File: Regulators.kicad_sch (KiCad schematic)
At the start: 22 parts, among them J5 24V Logic, J6 24V Isolated, U2 XL1509-12, U3 XL1509-5.0

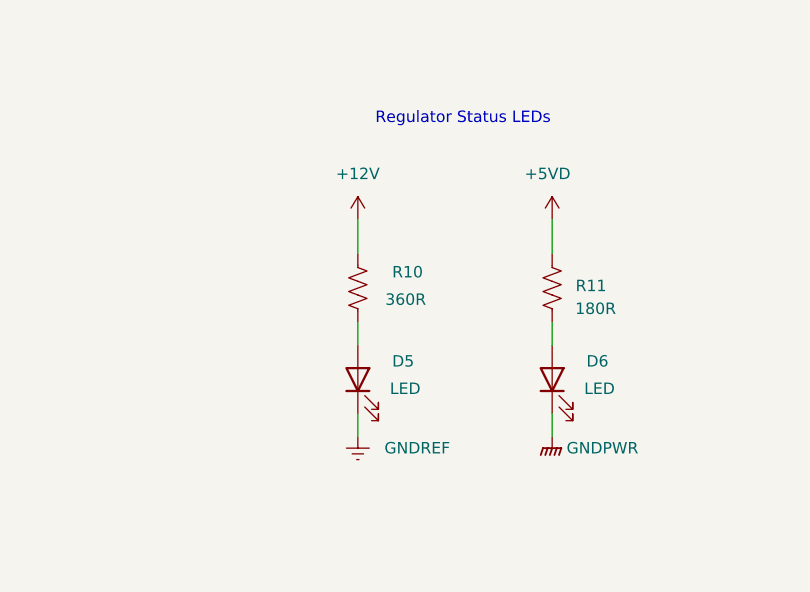
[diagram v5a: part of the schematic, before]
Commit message: Caught some errors with spacing of jumpers, did some BOM consolidation and included BOM. Updates to Gerbers to reflect new changes.
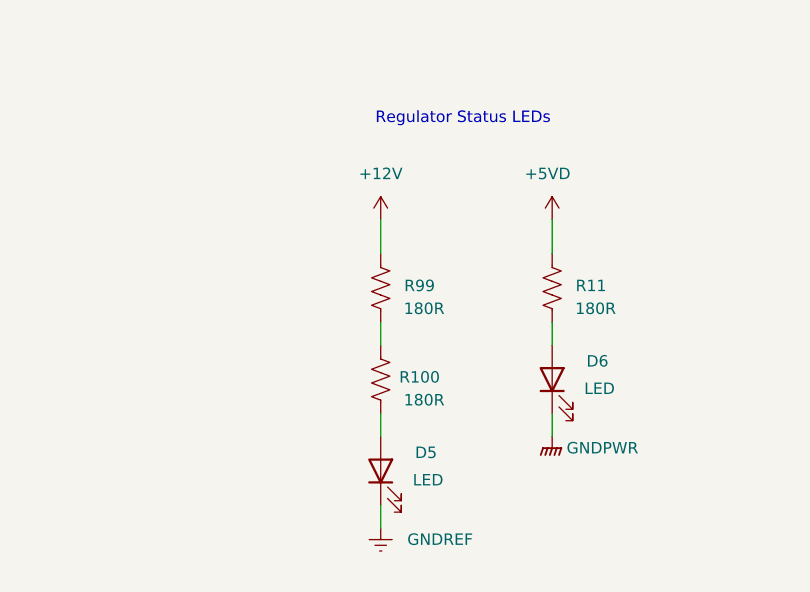
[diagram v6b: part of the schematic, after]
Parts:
- removed R10: 360R, Resistor_SMD:R_1206_3216Metric_Pad1.30x1.75mm_HandSolder, symbol Device:R_US
- added R100, R99: 180R, Resistor_SMD:R_1206_3216Metric_Pad1.30x1.75mm_HandSolder, symbol Device:R_US
- C3, C4: Digikey Part Number 493-12789-1-ND -> 493-1110-ND; Digikey URL https://www.digikey.com.au/en/products/detail/nichicon/UVR1H471MHD1TO/1978711 -> https://www.digikey.com.au/en/products/detail/nichicon/UVR1H471MHD/588851
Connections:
- net +12V: now also R99.1
- net at D5.2 (A): now also R100.2
- new net: R100.1, R99.2
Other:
- moved on the sheet: D5
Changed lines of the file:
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@@
 	(wire
 		(pts
+			(xy 217.17 120.65) (xy 217.17 123.19)
+		)
+		(stroke
+			(width 0)
+			(type default)
+		)
+	)
+	(wire
+		(pts
 			(xy 153.67 107.95) (xy 153.67 109.22)
 		)
@@
 	(wire
 		(pts
-			(xy 214.63 109.22) (xy 214.63 113.03)
+			(xy 217.17 109.22) (xy 217.17 113.03)
 		)
 		(stroke
@@
 	(wire
 		(pts
-			(xy 214.63 130.81) (xy 214.63 133.35)
+			(xy 217.17 140.97) (xy 217.17 143.51)
 		)
 		(stroke
@@
 	(wire
 		(pts
-			(xy 214.63 120.65) (xy 214.63 123.19)
+			(xy 217.17 130.81) (xy 217.17 133.35)
 		)
 		(stroke
@@
 	(symbol
 		(lib_id "power:+12V")
-		(at 214.63 109.22 0)
+		(at 217.17 109.22 0)
 		(unit 1)
 		(exclude_from_sim no)
@@
 		(fields_autoplaced yes)
 		(property "Reference" "#PWR054"
-			(at 214.63 113.03 0)
+			(at 217.17 113.03 0)
 			(effects
 				(font
@@
 		)
 		(property "Value" "+12V"
-			(at 214.63 104.14 0)
+			(at 217.17 104.14 0)
 			(effects
 				(font
@@
 		)
 		(property "Footprint" ""
-			(at 214.63 109.22 0)
+			(at 217.17 109.22 0)
 			(effects
 				(font
@@
 		)
 		(property "Datasheet" ""
-			(at 214.63 109.22 0)
+			(at 217.17 109.22 0)
 			(effects
 				(font
@@
 		)
 		(property "Description" "Power symbol creates a global label with name \"+12V\""
-			(at 214.63 109.22 0)
+			(at 217.17 109.22 0)
 			(effects
 				(font
@@
 	)
 	(symbol
+		(lib_id "Device:R_US")
+		(at 217.17 116.84 0)
+		(unit 1)
+		(exclude_from_sim no)
+		(in_bom yes)
+		(on_board yes)
+		(dnp no)
+		(property "Reference" "R99"
+			(at 221.488 116.586 0)
+			(effects
+				(font
+					(size 1.27 1.27)
+				)
+			)
+		)
+		(property "Value" "180R"
+			(at 221.996 119.126 0)
+			(effects
+				(font
+					(size 1.27 1.27)
+				)
+			)
+		)
+		(property "Footprint" "Resistor_SMD:R_1206_3216Metric_Pad1.30x1.75mm_HandSolder"
+			(at 218.186 117.094 90)
+			(effects
+				(font
+					(size 1.27 1.27)
+				)
+				(hide yes)
+			)
+		)
+		(property "Datasheet" "~"
+			(at 217.17 116.84 0)
+			(effects
+				(font
+					(size 1.27 1.27)
+				)
+				(hide yes)
+			)
+		)
+		(property "Description" "Resistor, US symbol"
+			(at 217.17 116.84 0)
+			(effects
+				(font
+					(size 1.27 1.27)
+				)
+				(hide yes)
+			)
+		)
+		(property "Digikey Part Number" "311-180FRCT-ND"
+			(at 217.17 116.84 0)
+			(effects
+				(font
+					(size 1.27 1.27)
+				)
+				(hide yes)
+			)
+		)
+		(property "Digikey URL" "https://www.digikey.com.au/en/products/detail/yageo/RC1206FR-07180RL/728597"
+			(at 217.17 116.84 0)
+			(effects
+				(font
+					(size 1.27 1.27)
+				)
+				(hide yes)
+			)
+		)
+		(pin "2"
+		)
+		(pin "1"
+		)
+		(instances
+			(project "Remora Nucleo F446ZE Hat"
+				(path "/5473abc6-7b93-43cc-a401-f691c4d7d7cf/e0dc83df-f7d9-4488-bd0b-6c0af36f8703"
+					(reference "R99")
+					(unit 1)
+				)
+			)
+		)
+	)
+	(symbol
 		(lib_id "power:+5VD")
 		(at 153.67 107.95 0)
@@
 	)
 	(symbol
+		(lib_id "Device:R_US")
+		(at 217.17 127 0)
+		(unit 1)
+		(exclude_from_sim no)
+		(in_bom yes)
+		(on_board yes)
+		(dnp no)
+		(property "Reference" "R100"
+			(at 221.488 126.746 0)
+			(effects
+				(font
+					(size 1.27 1.27)
+				)
+			)
+		)
+		(property "Value" "180R"
+			(at 221.996 129.286 0)
+			(effects
+				(font
+					(size 1.27 1.27)
+				)
+			)
+		)
+		(property "Footprint" "Resistor_SMD:R_1206_3216Metric_Pad1.30x1.75mm_HandSolder"
+			(at 218.186 127.254 90)
+			(effects
+				(font
+					(size 1.27 1.27)
+				)
+				(hide yes)
+			)
+		)
+		(property "Datasheet" "~"
+			(at 217.17 127 0)
+			(effects
+				(font
+					(size 1.27 1.27)
+				)
+				(hide yes)
+			)
+		)
+		(property "Description" "Resistor, US symbol"
+			(at 217.17 127 0)
+			(effects
+				(font
+					(size 1.27 1.27)
+				)
+				(hide yes)
+			)
+		)
+		(property "Digikey Part Number" "311-180FRCT-ND"
+			(at 217.17 127 0)
+			(effects
+				(font
+					(size 1.27 1.27)
+				)
+				(hide yes)
+			)
+		)
+		(property "Digikey URL" "https://www.digikey.com.au/en/products/detail/yageo/RC1206FR-07180RL/728597"
+			(at 217.17 127 0)
+			(effects
+				(font
+					(size 1.27 1.27)
+				)
+				(hide yes)
+			)
+		)
+		(pin "2"
+		)
+		(pin "1"
+		)
+		(instances
+			(project "Remora Nucleo F446ZE Hat"
+				(path "/5473abc6-7b93-43cc-a401-f691c4d7d7cf/e0dc83df-f7d9-4488-bd0b-6c0af36f8703"
+					(reference "R100")
+					(unit 1)
+				)
+			)
+		)
+	)
+	(symbol
 		(lib_id "Device:C_Polarized")
 		(at 63.5 127 0)
@@
 			)
 		)
-		(property "Digikey Part Number" "493-12789-1-ND"
+		(property "Digikey Part Number" "493-1110-ND"
 			(at 63.5 127 0)
 			(effects
@@
 			)
 		)
-		(property "Digikey URL" "https://www.digikey.com.au/en/products/detail/nichicon/UVR1H471MHD1TO/1978711"
+		(property "Digikey URL" "https://www.digikey.com.au/en/products/detail/nichicon/UVR1H471MHD/588851"
 			(at 63.5 127 0)
 			(effects
@@
 	(symbol
 		(lib_id "Device:LED")
-		(at 214.63 127 90)
+		(at 217.17 137.16 90)
 		(unit 1)
 		(exclude_from_sim no)
@@
 		(dnp no)
 		(property "Reference" "D5"
-			(at 218.44 124.968 90)
+			(at 220.98 135.128 90)
 			(effects
 				(font
@@
 		)
 		(property "Value" "LED"
-			(at 218.186 128.016 90)
+			(at 220.726 138.176 90)
 			(effects
 				(font
@@
 		)
 		(property "Footprint" "Diode_SMD:D_1206_3216Metric_Pad1.42x1.75mm_HandSolder"
-			(at 214.63 127 0)
+			(at 217.17 137.16 0)
 			(effects
 				(font
@@
 		)
 		(property "Datasheet" "~"
-			(at 214.63 127 0)
+			(at 217.17 137.16 0)
 			(effects
 				(font
@@
 		)
 		(property "Description" "Light emitting diode"
-			(at 214.63 127 0)
+			(at 217.17 137.16 0)
 			(effects
 				(font
@@
 		)
 		(property "Sim.Pins" "1=K 2=A"
-			(at 214.63 127 0)
+			(at 217.17 137.16 0)
 			(effects
 				(font
@@
 		)
 		(property "Digikey Part Number" "3147-B1501USD-20D000313U1930CT-ND "
-			(at 214.63 127 0)
+			(at 217.17 137.16 0)
 			(effects
 				(font
@@
 		)
 		(property "Digikey URL" "https://www.digikey.com.au/en/products/detail/harvatek-corporation/B1501USD-20D000313U1930/24635249 "
-			(at 214.63 127 0)
+			(at 217.17 137.16 0)
 			(effects
 				(font
@@
 	(symbol
 		(lib_id "power:GNDREF")
-		(at 214.63 133.35 0)
+		(at 217.17 143.51 0)
 		(unit 1)
 		(exclude_from_sim no)
@@
 		(dnp no)
 		(property "Reference" "#PWR055"
-			(at 214.63 139.7 0)
+			(at 217.17 149.86 0)
 			(effects
 				(font
@@
 		)
 		(property "Value" "GNDREF"
-			(at 221.234 134.62 0)
+			(at 223.774 144.78 0)
 			(effects
 				(font
@@
 		)
 		(property "Footprint" ""
-			(at 214.63 133.35 0)
+			(at 217.17 143.51 0)
 			(effects
 				(font
@@
 		)
 		(property "Datasheet" ""
-			(at 214.63 133.35 0)
+			(at 217.17 143.51 0)
 			(effects
 				(font
@@
 		)
 		(property "Description" "Power symbol creates a global label with name \"GNDREF\" , reference supply ground"
-			(at 214.63 133.35 0)
+			(at 217.17 143.51 0)
 			(effects
 				(font
@@
 			)
 		)
-		(property "Digikey Part Number" "493-12789-1-ND"
+		(property "Digikey Part Number" "493-1110-ND"
 			(at 63.5 57.15 0)
 			(effects
@@
 			)
 		)
-		(property "Digikey URL" "https://www.digikey.com.au/en/products/detail/nichicon/UVR1H471MHD1TO/1978711"
+		(property "Digikey URL" "https://www.digikey.com.au/en/products/detail/nichicon/UVR1H471MHD/588851"
 			(at 63.5 57.15 0)
 			(effects
@@
 					(unit 1)
 				)
-			)
-		)
-	)
-	(symbol
-		(lib_id "Device:R_US")
-		(at 214.63 116.84 0)
-		(unit 1)
-		(exclude_from_sim no)
-		(in_bom yes)
-		(on_board yes)
-		(dnp no)
-		(property "Reference" "R10"
-			(at 218.44 115.062 0)
-			(effects
-				(font
-					(size 1.27 1.27)
-				)
-				(justify left)
-			)
-		)
-		(property "Value" "360R"
-			(at 217.678 118.11 0)
-			(effects
-				(font
-					(size 1.27 1.27)
-				)
-				(justify left)
-			)
-		)
-		(property "Footprint" "Resistor_SMD:R_1206_3216Metric_Pad1.30x1.75mm_HandSolder"
-			(at 215.646 117.094 90)
-			(effects
-				(font
-					(size 1.27 1.27)
-				)
-				(hide yes)
-			)
-		)
-		(property "Datasheet" "~"
-			(at 214.63 116.84 0)
-			(effects
-				(font
-					(size 1.27 1.27)
-				)
-				(hide yes)
-			)
-		)
-		(property "Description" "Resistor, US symbol"
-			(at 214.63 116.84 0)
-			(effects
-				(font
-					(size 1.27 1.27)
-				)
-				(hide yes)
-			)
-		)
-		(property "Digikey Part Number" "RMCF1206JT360RCT-ND"
-			(at 214.63 116.84 0)
-			(effects
-				(font
-					(size 1.27 1.27)
-				)
-				(hide yes)
-			)
-		)
-		(property "Digikey URL" "https://www.digikey.com.au/en/products/detail/stackpole-electronics-inc/RMCF1206JT360R/1753824"
-			(at 214.63 116.84 0)
-			(effects
-				(font
-					(size 1.27 1.27)
-				)
-				(hide yes)
-			)
-		)
-		(pin "1"
-		)
-		(pin "2"
-		)
-		(instances
-			(project "Remora Nucleo F446RE Hat"
-				(path "/5473abc6-7b93-43cc-a401-f691c4d7d7cf/e0dc83df-f7d9-4488-bd0b-6c0af36f8703"
-					(reference "R10")
-					(unit 1)
-				)

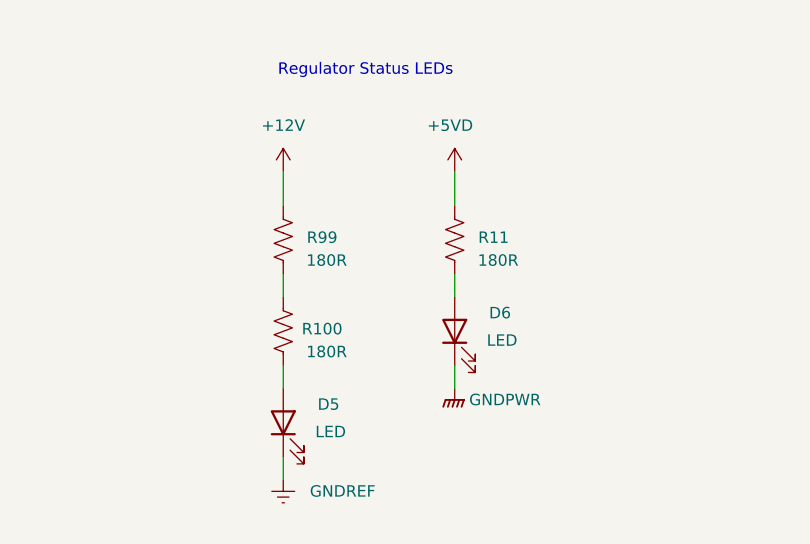
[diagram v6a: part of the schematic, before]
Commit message: Some file changes and output new gerbers + BOM and centroid file for PCBWay Order
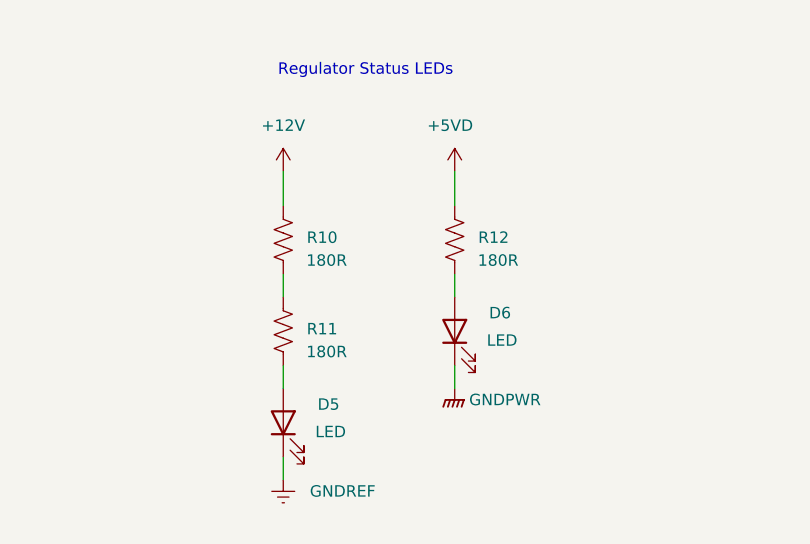
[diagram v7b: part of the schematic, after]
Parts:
- renumbered R99 to R10, R100 to R11, R11 to R12
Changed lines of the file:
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@@
 		(on_board yes)
 		(dnp no)
-		(property "Reference" "R99"
+		(property "Reference" "R10"
 			(at 221.488 116.586 0)
 			(effects
@@
 			(project "Remora Nucleo F446ZE Hat"
 				(path "/5473abc6-7b93-43cc-a401-f691c4d7d7cf/e0dc83df-f7d9-4488-bd0b-6c0af36f8703"
-					(reference "R99")
+					(reference "R10")
 					(unit 1)
 				)
@@
 		(on_board yes)
 		(dnp no)
-		(property "Reference" "R100"
+		(property "Reference" "R11"
 			(at 221.488 126.746 0)
 			(effects
@@
 			(project "Remora Nucleo F446ZE Hat"
 				(path "/5473abc6-7b93-43cc-a401-f691c4d7d7cf/e0dc83df-f7d9-4488-bd0b-6c0af36f8703"
-					(reference "R100")
+					(reference "R11")
 					(unit 1)
 				)
@@
 		(on_board yes)
 		(dnp no)
-		(property "Reference" "R11"
+		(property "Reference" "R12"
 			(at 240.538 116.586 0)
 			(effects
@@
 			(project "Remora Nucleo F446ZE Hat"
 				(path "/5473abc6-7b93-43cc-a401-f691c4d7d7cf/e0dc83df-f7d9-4488-bd0b-6c0af36f8703"
-					(reference "R11")
-					(unit 1)
-				)
+					(reference "R12")
+					(unit 1)
+				)

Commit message: Fixed found issue with oversized regulator input cap
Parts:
- C3, C4: footprint Capacitor_THT:CP_Radial_D8.0mm_P3.50mm -> Capacitor_THT:CP_Radial_D10.0mm_P5.00mm; Digikey Part Number 493-1110-ND -> 399-ESK477M050AH4KACT-ND; Digikey URL https://www.digikey.com.au/en/products/detail/nichicon/UVR1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 -> https://www.digikey.com/en/products/detail/kemet/ESK477M050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
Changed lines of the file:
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@@
 			)
 		)
-		(property "Footprint" "Capacitor_THT:CP_Radial_D8.0mm_P3.50mm"
+		(property "Footprint" "Capacitor_THT:CP_Radial_D10.0mm_P5.00mm"
 			(at 64.4652 130.81 0)
 			(effects
@@
 			)
 		)
-		(property "Digikey Part Number" "493-1110-ND"
+		(property "Digikey Part Number" "399-ESK477M050AH4KACT-ND"
 			(at 63.5 127 0)
 			(effects
@@
 			)
 		)
-		(property "Digikey URL" "https://www.digikey.com.au/en/products/detail/nichicon/UVR1H471MHD/588851"
+		(property "Digikey URL" "https://www.digikey.com/en/products/detail/kemet/ESK477M050AH4KA/13176396"
 			(at 63.5 127 0)
 			(effects
@@
 			)
 		)
-		(property "Footprint" "Capacitor_THT:CP_Radial_D8.0mm_P3.50mm"
+		(property "Footprint" "Capacitor_THT:CP_Radial_D10.0mm_P5.00mm"
 			(at 64.4652 60.96 0)
 			(effects
@@
 			)
 		)
-		(property "Digikey Part Number" "493-1110-ND"
+		(property "Digikey Part Number" "399-ESK477M050AH4KACT-ND"
 			(at 63.5 57.15 0)
 			(effects
@@
 			)
 		)
-		(property "Digikey URL" "https://www.digikey.com.au/en/products/detail/nichicon/UVR1H471MHD/588851"
+		(property "Digikey URL" "https://www.digikey.com/en/products/detail/kemet/ESK477M050AH4KA/13176396"
 			(at 63.5 57.15 0)
 			(effects
